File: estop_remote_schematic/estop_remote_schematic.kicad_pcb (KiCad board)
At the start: 2 copper layers, 60 x 75 mm, 24 parts, among them J1 Power Switch, J2 ESP32 Pins 1-22, J3 ESP32 Pins 23-44, J4 Battery Connector, J5 EStop Button, J6 OLed Screen Pins, J7 HC12 Connections, J8 Reset Button, J9 RotaryEnc Connections

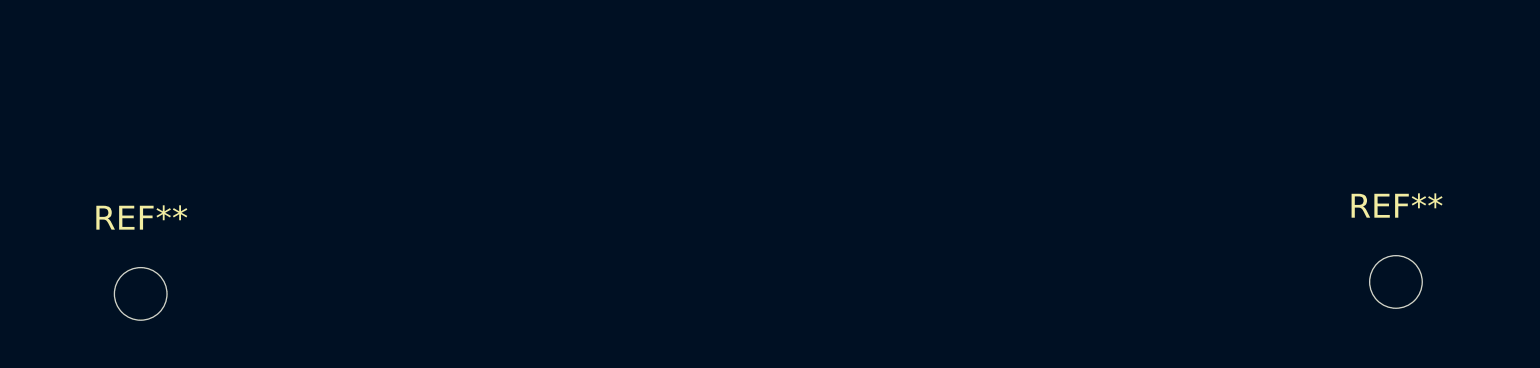
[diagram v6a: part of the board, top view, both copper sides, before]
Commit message: Updated silkscreen of PCB to have RPI Robotics Logo and name of PCB
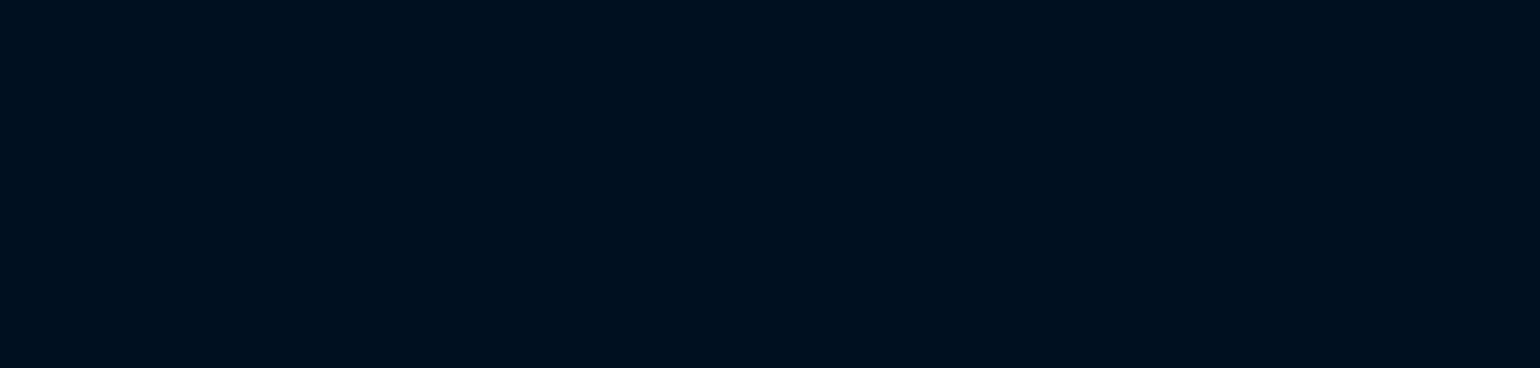
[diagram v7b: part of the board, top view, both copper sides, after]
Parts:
- removed the REF** at (71.5, 178.5)
- removed the REF** at (124.0, 178.0)
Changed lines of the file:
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@@
 		)
-	)
-	(footprint "MountingHole:MountingHole_2.2mm_M2"
-		(layer "F.Cu")
-		(at 71.5 178.5)
-		(descr "Mounting Hole 2.2mm, M2, no annular, generated by kicad-footprint-generator mountinghole.py")
-		(tags "mountinghole M2")
-		(property "Reference" "REF**"
-			(at 0 -3.15 0)
-			(layer "F.SilkS")
-			(effects
-				(font
-					(size 1 1)
-					(thickness 0.15)
-				)
-			)
-		)
-		(property "Value" "MountingHole_2.2mm_M2"
-			(at 0 3.15 0)
-			(layer "F.Fab")
-			(effects
-				(font
-					(size 1 1)
-					(thickness 0.15)
-				)
-			)
-		)
-		(property "Datasheet" ""
-			(at 0 0 0)
-			(layer "F.Fab")
-			(hide yes)
-			(effects
-				(font
-					(size 1.27 1.27)
-				)
-			)
-		)
-		(property "Description" ""
-			(at 0 0 0)
-			(layer "F.Fab")
-			(hide yes)
-			(effects
-				(font
-					(size 1.27 1.27)
-				)
-			)
-		)
-		(property "KiLib_Generator" "mounting_hardware/mounting_hole"
-			(at 0 0 0)
-			(layer "F.SilkS")
-			(hide yes)
-			(effects
-				(font
-					(size 1 1)
-					(thickness 0.15)
-				)
-			)
-		)
-		(attr exclude_from_pos_files exclude_from_bom)
-		(duplicate_pad_numbers_are_jumpers no)
-		(fp_circle
-			(center 0 0)
-			(end 2.2 0)
-			(stroke
-				(width 0.15)
-				(type solid)
-			)
-			(fill no)
-			(layer "Cmts.User")
-		)
-		(fp_circle
-			(center 0 0)
-			(end 2.45 0)
-			(stroke
-				(width 0.05)
-				(type solid)
-			)
-			(fill no)
-			(layer "F.CrtYd")
-		)
-		(fp_text user "${REFERENCE}"
-			(at 0 0 0)
-			(layer "F.Fab")
-			(effects
-				(font
-					(size 1 1)
-					(thickness 0.15)
-				)
-			)
-		)
-		(pad "" np_thru_hole circle
-			(at 0 0)
-			(size 2.2 2.2)
-			(drill 2.2)
-			(layers "*.Cu" "*.Mask")
-		)
-		(embedded_fonts no)
 	)
 	(footprint "Resistor_SMD:R_0805_2012Metric_Pad1.20x1.40mm_HandSolder"
@@
 		)
 	)
-	(footprint "MountingHole:MountingHole_2.2mm_M2"
-		(layer "F.Cu")
-		(at 124 178)
-		(descr "Mounting Hole 2.2mm, M2, no annular, generated by kicad-footprint-generator mountinghole.py")
-		(tags "mountinghole M2")
-		(property "Reference" "REF**"
-			(at 0 -3.15 0)
-			(layer "F.SilkS")
-			(effects
-				(font
-					(size 1 1)
-					(thickness 0.15)
-				)
-			)
-		)
-		(property "Value" "MountingHole_2.2mm_M2"
-			(at 0 3.15 0)
-			(layer "F.Fab")
-			(effects
-				(font
-					(size 1 1)
-					(thickness 0.15)
-				)
-			)
-		)
-		(property "Datasheet" ""
-			(at 0 0 0)
-			(layer "F.Fab")
-			(hide yes)
-			(effects
-				(font
-					(size 1.27 1.27)
-				)
-			)
-		)
-		(property "Description" ""
-			(at 0 0 0)
-			(layer "F.Fab")
-			(hide yes)
-			(effects
-				(font
-					(size 1.27 1.27)
-				)
-			)
-		)
-		(property "KiLib_Generator" "mounting_hardware/mounting_hole"
-			(at 0 0 0)
-			(layer "F.SilkS")
-			(hide yes)
-			(effects
-				(font
-					(size 1 1)
-					(thickness 0.15)
-				)
-			)
-		)
-		(attr exclude_from_pos_files exclude_from_bom)
-		(duplicate_pad_numbers_are_jumpers no)
-		(fp_circle
-			(center 0 0)
-			(end 2.2 0)
-			(stroke
-				(width 0.15)
-				(type solid)
-			)
-			(fill no)
-			(layer "Cmts.User")
-		)
-		(fp_circle
-			(center 0 0)
-			(end 2.45 0)
-			(stroke
-				(width 0.05)
-				(type solid)
-			)
-			(fill no)
-			(layer "F.CrtYd")
-		)
-		(fp_text user "${REFERENCE}"
-			(at 0 0 0)
-			(layer "F.Fab")
-			(effects
-				(font
-					(size 1 1)
-					(thickness 0.15)
-				)
-			)
-		)
-		(pad "" np_thru_hole circle
-			(at 0 0)
-			(size 2.2 2.2)
-			(drill 2.2)
-			(layers "*.Cu" "*.Mask")
-		)
-		(embedded_fonts no)
-	)
 	(footprint "Connector_PinSocket_2.54mm:PinSocket_1x22_P2.54mm_Vertical"

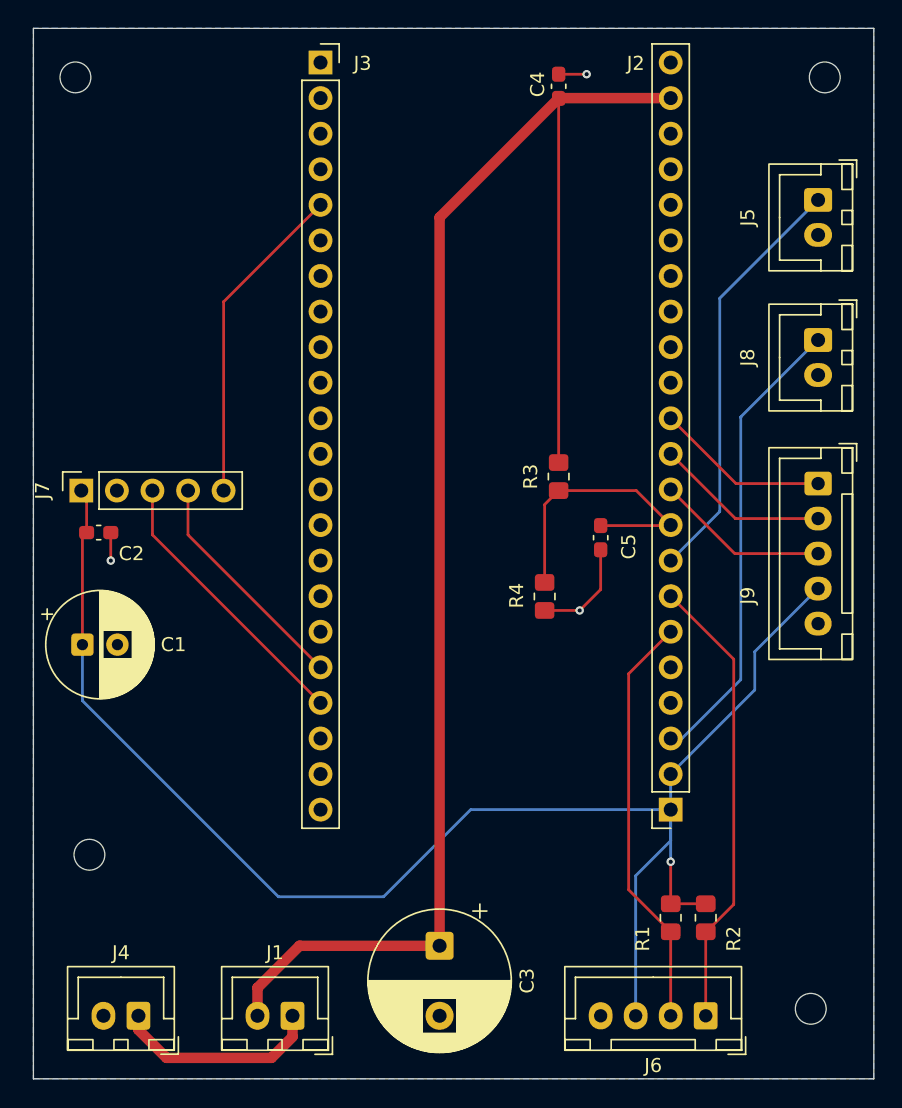
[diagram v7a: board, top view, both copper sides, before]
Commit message: Modified values on components to be more standardized
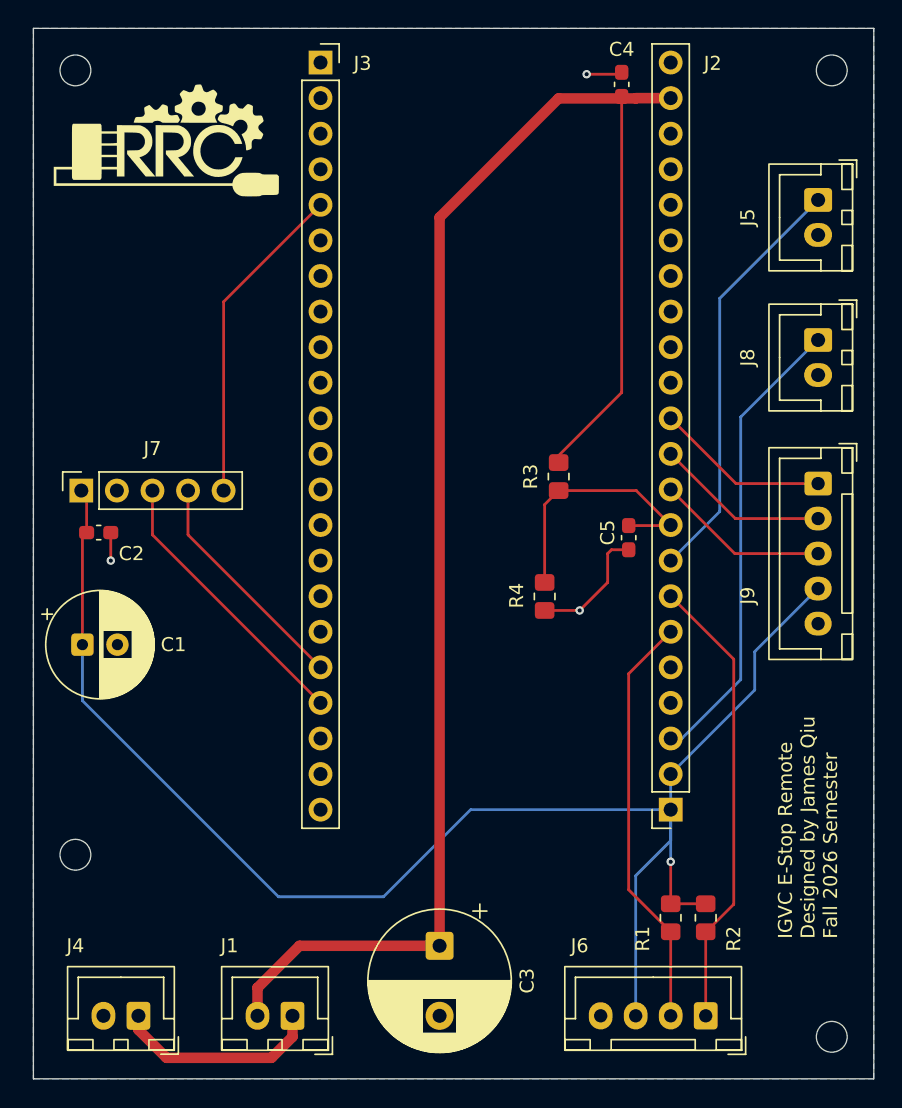
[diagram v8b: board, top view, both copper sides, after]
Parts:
- added G***: LOGO, RPI-Robotics:RPIR-LOGO-8x16, F.Cu at (77.5, 40.0)
- J1: value Power Switch -> JST-XH-2A
- J2: value ESP32 Pins 1-22 -> Conn_01x22
- J3: value ESP32 Pins 23-44 -> Conn_01x22
- J4: value Battery Connector -> JST-XH-2A
- J5: value EStop Button -> JST-XH-2A
- J6: value OLed Screen Pins -> Conn_01x04
- J8: value Reset Button -> JST-XH-2A
- J9: value RotaryEnc Connections -> JST-XH-5A
- moved C4 4.50 mm to (110.0, 36.0)
- moved REF** 2.50 mm to (125.0, 104.0)
- moved C5 2.00 mm to (110.5, 68.4)
- moved REF** 1.00 mm to (71.0, 91.0)
- moved REF** 0.71 mm to (125.0, 35.0)
- moved REF** 0.50 mm to (71.0, 35.0)
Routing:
- net +6V: track 114.3 -> 116.4 mm
- net GND: track 11.5 -> 13.6 mm
- net /BatteryVoltageDivider: track 21.0 -> 19.0 mm
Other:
- board text added: "IGVC E-Stop Remote Designed by James Qiu Fall 2026 Semester"
